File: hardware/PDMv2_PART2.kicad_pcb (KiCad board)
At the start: 4 copper layers, 62 x 42.5 mm, 5 parts, among them J1 IPBS-110-01-XX-D-GP, J2 TVP00WCI17-02P

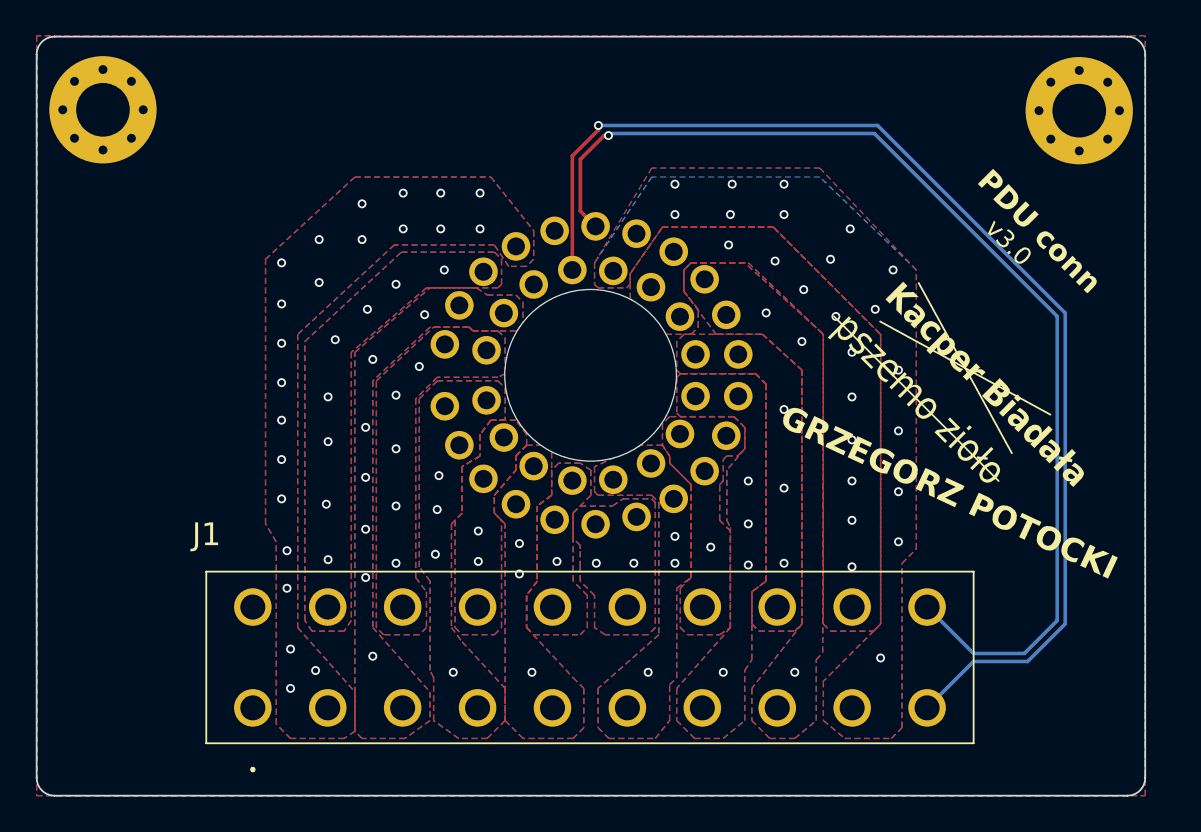
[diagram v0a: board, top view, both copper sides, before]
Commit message: can copied from steeringwheel
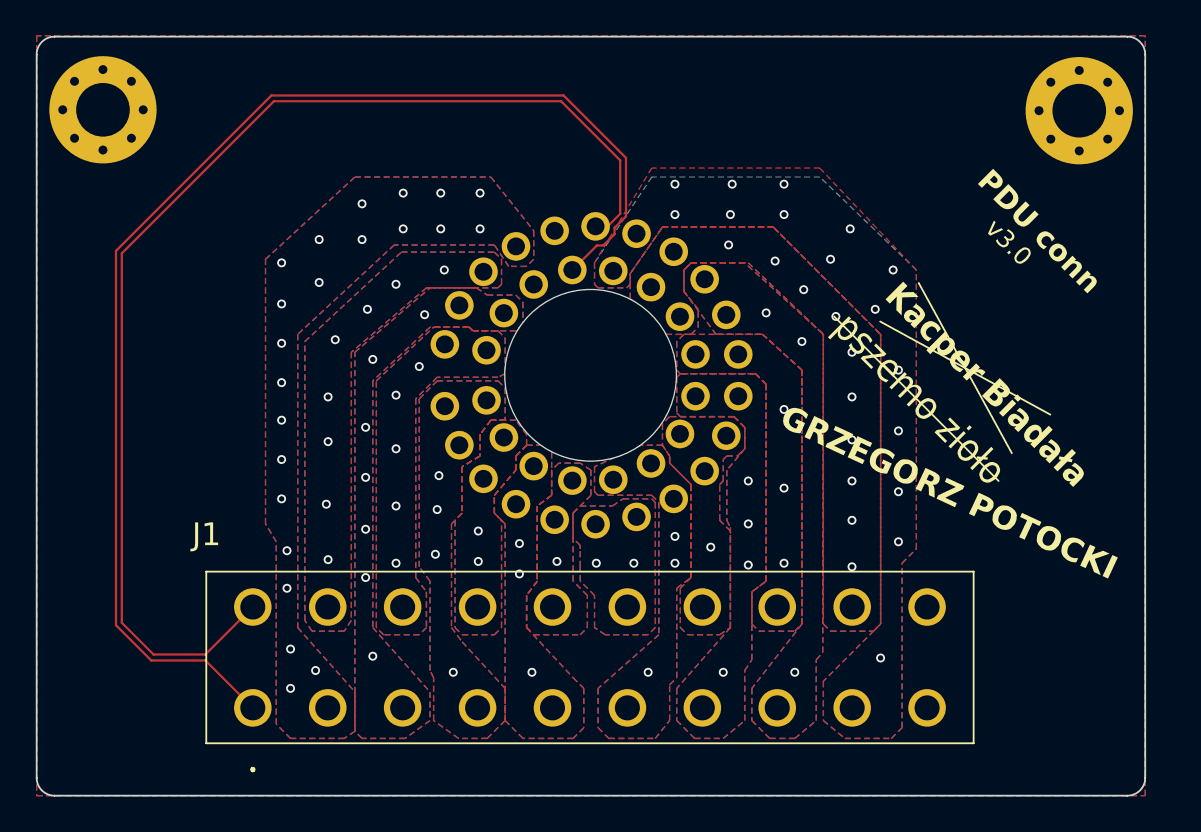
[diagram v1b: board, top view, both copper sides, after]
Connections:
- J1 pad 1: unconnected-(J1-Pad1) -> /CAN.P
- J1 pad 10: /CAN.P -> unconnected-(J1-Pad10)
- J1 pad 11: GND -> /CAN.N
- J1 pad 20: /CAN.N -> GND
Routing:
- net /CAN.P: track 66.2 -> 71.8 mm, vias 1 -> 0
- net /CAN.N: track 61.7 -> 67.2 mm, vias 1 -> 0
